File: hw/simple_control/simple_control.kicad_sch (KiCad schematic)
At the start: 1 part, among them J1 Screw_Terminal_01x02

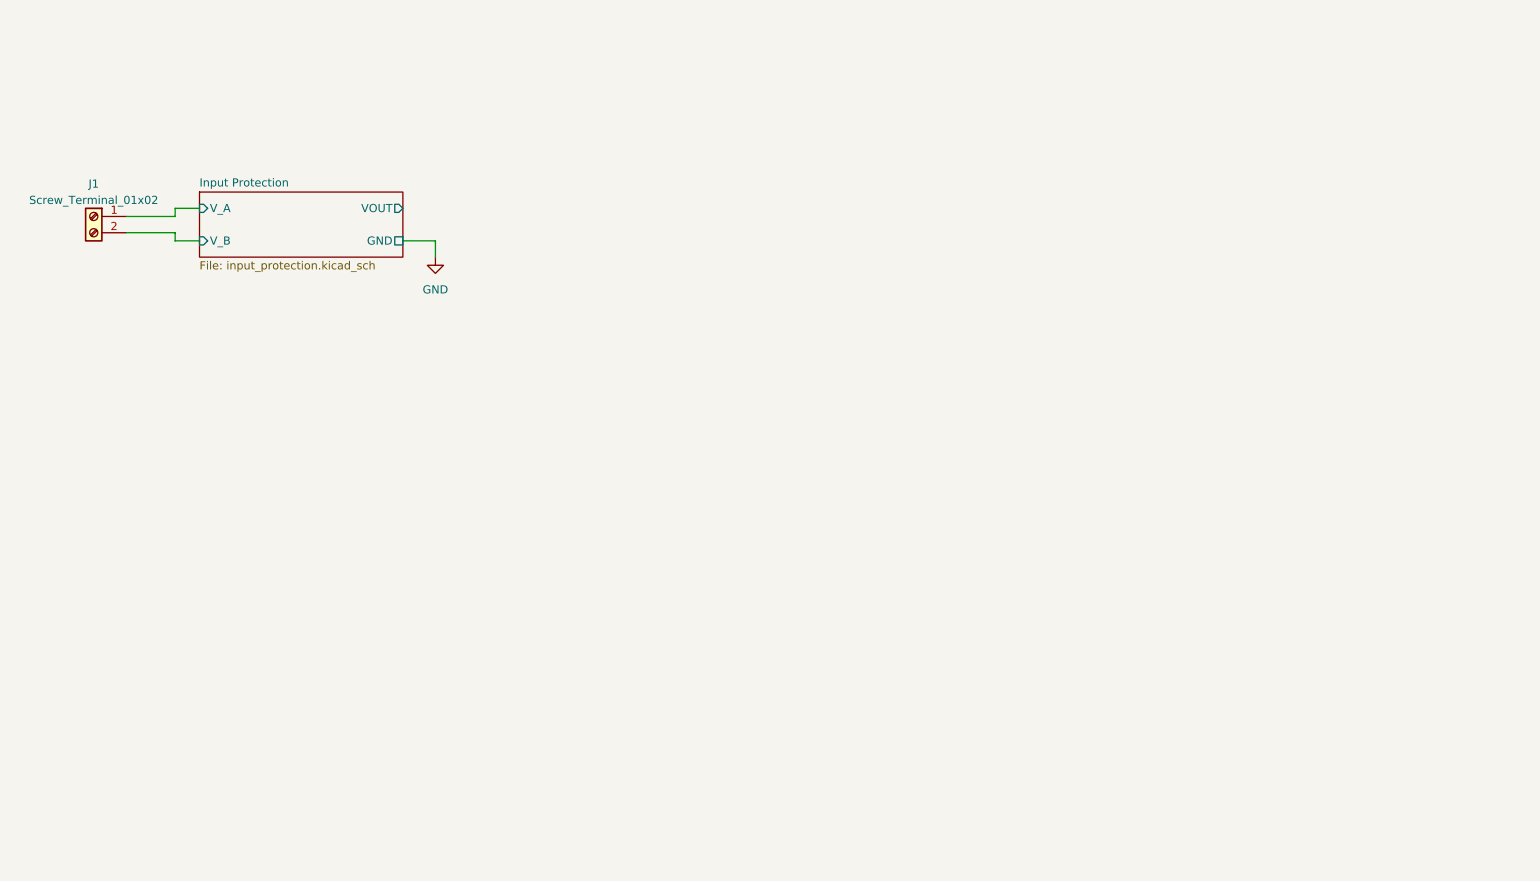
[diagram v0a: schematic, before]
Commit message: [hw] Add simple control LED driver
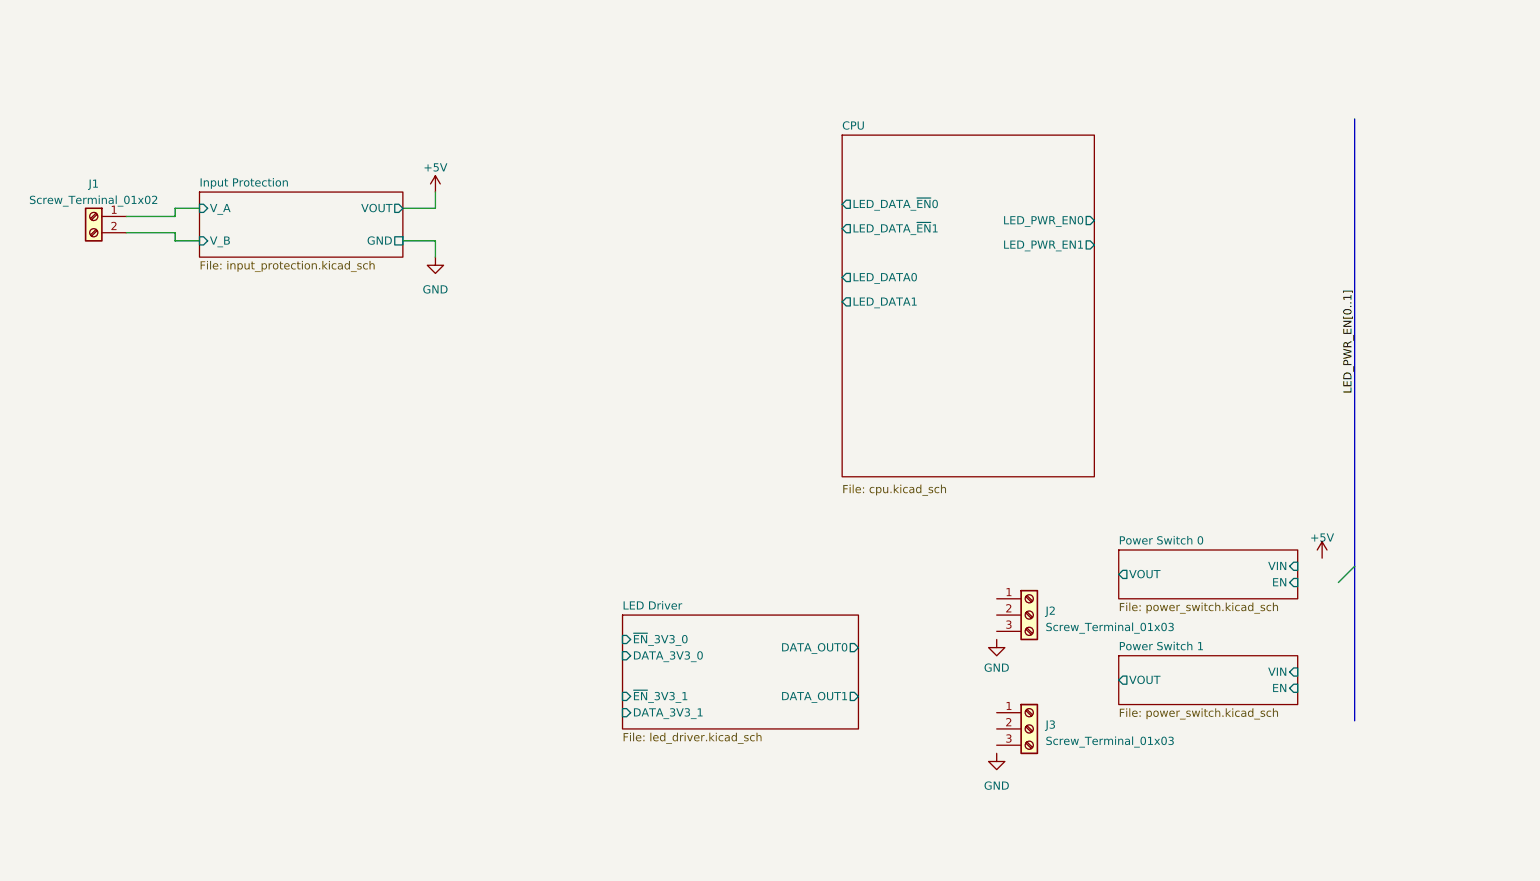
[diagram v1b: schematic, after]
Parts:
- added J2, J3: Screw_Terminal_01x03, symbol Connector:Screw_Terminal_01x03
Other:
- added sheet CPU (cpu.kicad_sch)
- added sheet LED Driver (led_driver.kicad_sch)
- added sheet Power Switch 0 (power_switch.kicad_sch)
- added sheet Power Switch 1 (power_switch.kicad_sch)

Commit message: [hw] Complete root schematics of simple control
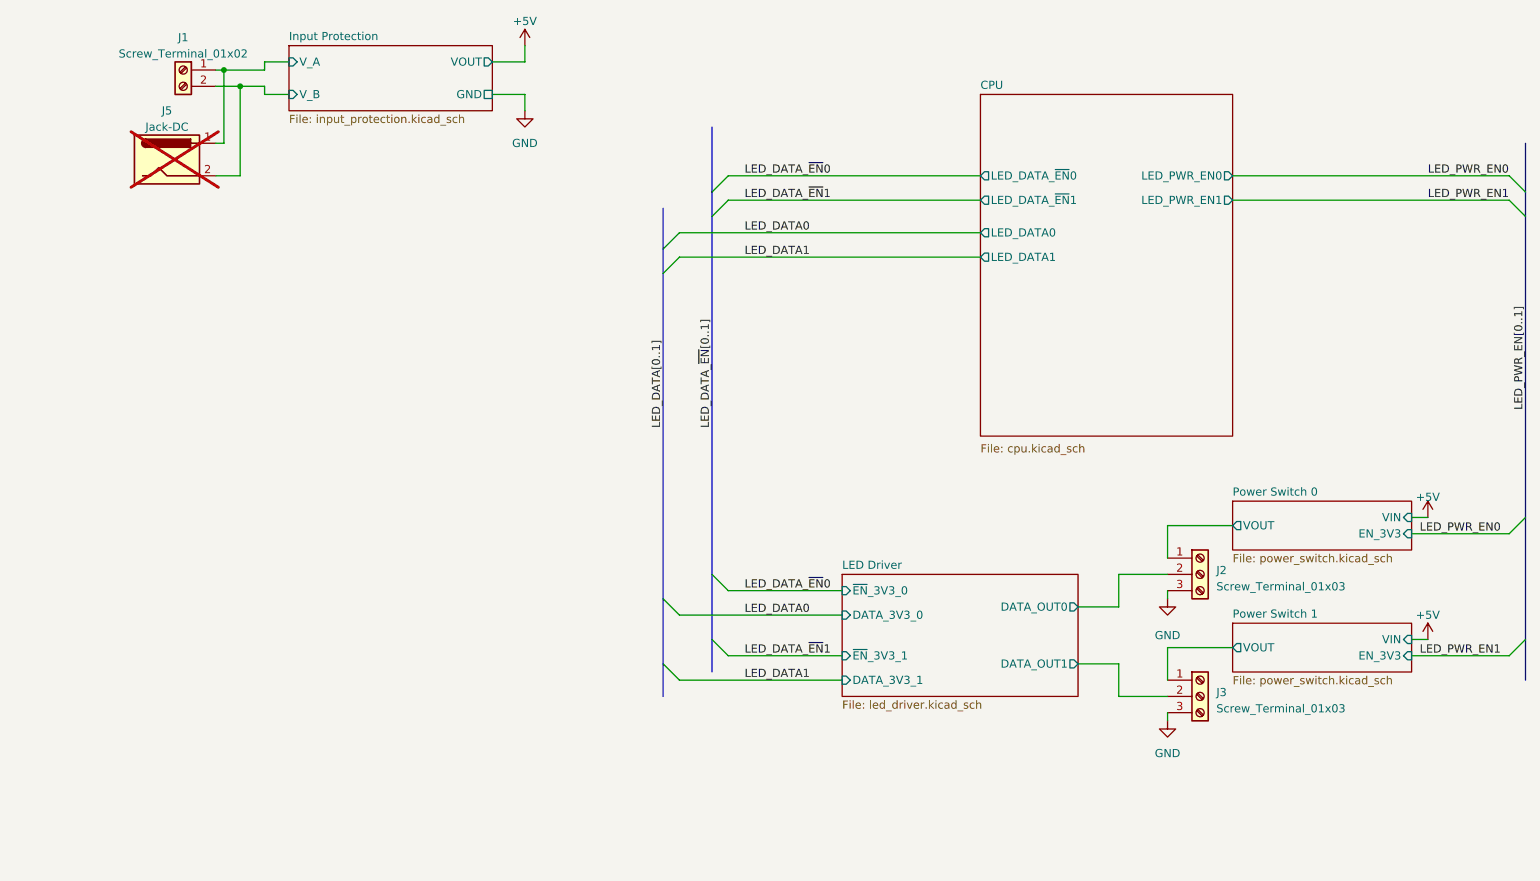
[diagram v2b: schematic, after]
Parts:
- added J5: Jack-DC, symbol Connector:Jack-DC
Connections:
- net GND: now also J2.3 (Pin_3), J3.3 (Pin_3)
- net Input Protection/V_A: now also J5.1
- net Input Protection/V_B: now also J5.2
- net LED Driver/DATA_OUT0: now also J2.2 (Pin_2)
- net LED Driver/DATA_OUT1: now also J3.2 (Pin_2)
- net Power Switch 0/VOUT: now also J2.1 (Pin_1)
- net Power Switch 1/VOUT: now also J3.1 (Pin_1)
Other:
- sheet Power Switch 0 ports: added EN_3V3; removed EN
- sheet Power Switch 1 ports: added EN_3V3; removed EN
- company: (none) -> Stefan Misik
- title: (none) -> WS2812 Simple Controller
- moved on the sheet: J1, J2, J3

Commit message: [hw] Wire some RPi Pico/Zero connections
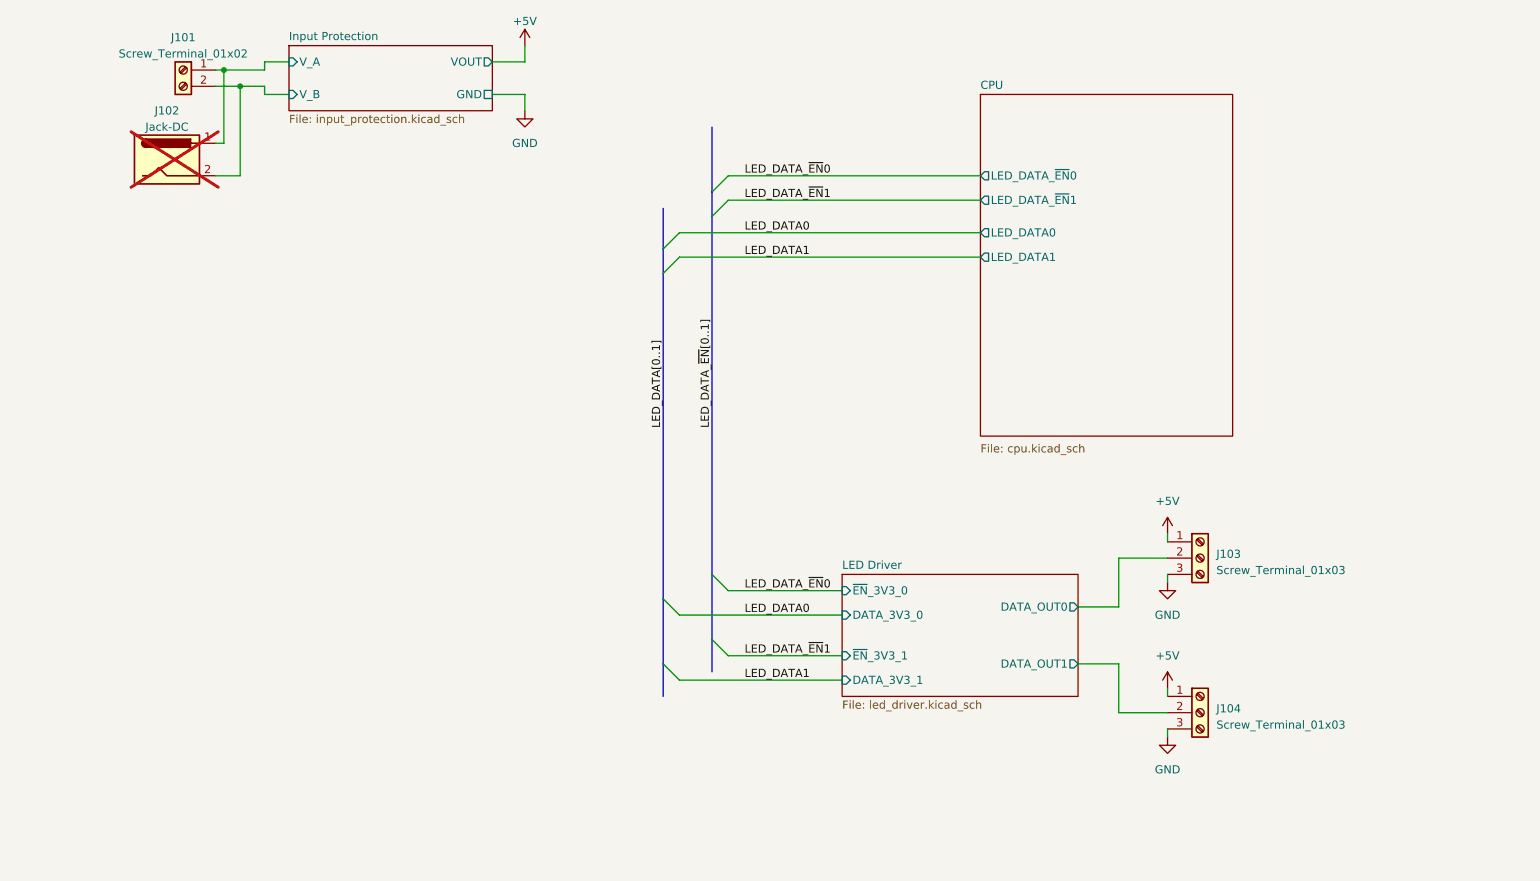
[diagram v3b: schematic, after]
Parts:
- renumbered J1 to J101, J5 to J102, J2 to J103, J3 to J104
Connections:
- net Power Switch 0/VOUT is gone; now on net +5V: J103.1 (Pin_1)
- net Power Switch 1/VOUT is gone; now on net +5V: J104.1 (Pin_1)
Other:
- removed sheet Power Switch 0
- removed sheet Power Switch 1
- sheet CPU ports: added none; removed LED_PWR_EN0, LED_PWR_EN1
- moved on the sheet: J103, J104

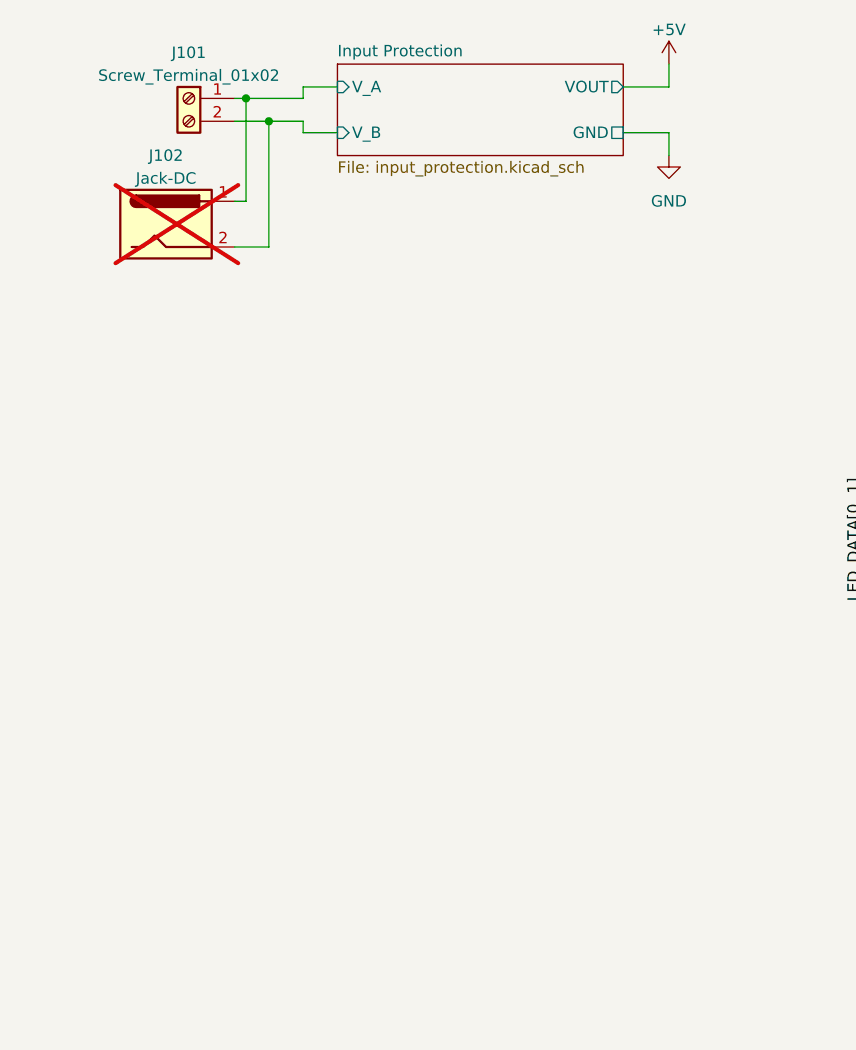
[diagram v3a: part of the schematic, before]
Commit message: [hw] Fix ERC issues, update RPi Pico library
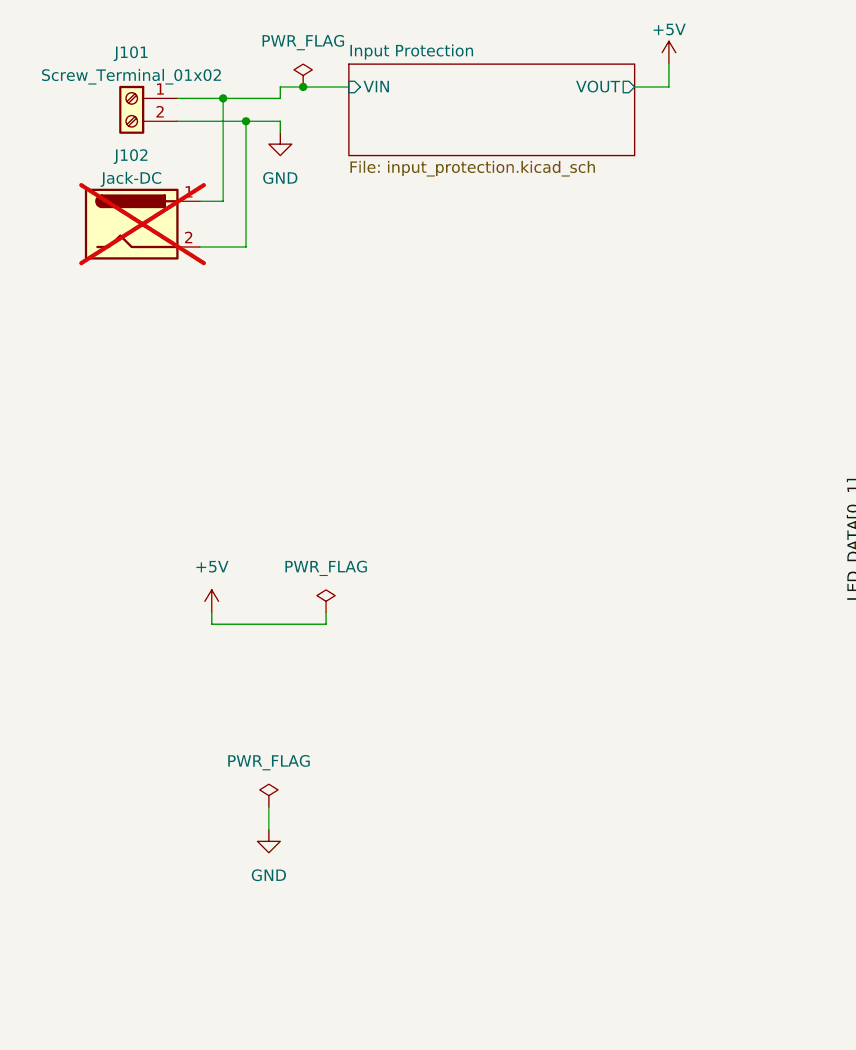
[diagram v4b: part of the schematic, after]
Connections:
- net Input Protection/V_B is gone; now on net GND: J101.2 (Pin_2), J102.2
- net Input Protection/V_A renamed Input Protection/VIN
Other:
- sheet Input Protection ports: added VIN; removed GND, V_A, V_B
- moved on the sheet: J101, J102

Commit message: chore(hw): assign footprints
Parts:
- J101: footprint (none) -> TerminalBlock_Phoenix:TerminalBlock_Phoenix_MKDS-1,5-2_1x02_P5.00mm_Horizontal
- J102: footprint (none) -> Connector_BarrelJack:BarrelJack_GCT_DCJ200-10-A_Horizontal; symbol Connector:Jack-DC -> Connector:Barrel_Jack_Switch; now in the parts list
- J103, J104: footprint (none) -> TerminalBlock_Phoenix:TerminalBlock_Phoenix_MKDS-1,5-3_1x03_P5.00mm_Horizontal
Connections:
- no-connect marks 0 -> 1
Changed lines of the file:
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@@
   (junction (at 50.8 45.72) (diameter 0) (color 0 0 0 0)
   )
+  (no_connect (at 39.37 60.96))
   (bus_entry (at 120.65 125.73) (size 2.54 2.54)
     (stroke (width 0) (type default))
@@
       (effects (font (size 1.27 1.27)) (justify left))
     )
-    (property "Footprint" "" (at 196.85 123.19 0)
+    (property "Footprint" "TerminalBlock_Phoenix:TerminalBlock_Phoenix_MKDS-1,5-3_1x03_P5.00mm_Horizontal" (at 196.85 123.19 0)
       (effects (font (size 1.27 1.27)) hide)
     )
@@
       (effects (font (size 1.27 1.27)))
     )
-    (property "Footprint" "" (at 31.75 46.99 0)
+    (property "Footprint" "TerminalBlock_Phoenix:TerminalBlock_Phoenix_MKDS-1,5-2_1x02_P5.00mm_Horizontal" (at 31.75 46.99 0)
       (effects (font (size 1.27 1.27)) hide)
     )
@@
   (symbol (lib_id "power:+5V") (at 40.64 104.14 0) (unit 1)
     (in_bom yes) (on_board yes) (dnp no) (fields_autoplaced)
-    (property "Reference" "#PWR0107" (at 40.64 107.95 0)
+    (property "Reference" "#PWR0103" (at 40.64 107.95 0)
       (effects (font (size 1.27 1.27)) hide)
     )
@@
       (project "simple_control"
         (path "/063164e8-0d2a-492b-8a61-e4fa4fbf06a6"
-          (reference "#PWR0107") (unit 1)
+          (reference "#PWR0103") (unit 1)
         )
       )
@@
   (symbol (lib_id "power:PWR_FLAG") (at 46.99 125.73 0) (unit 1)
     (in_bom yes) (on_board yes) (dnp no) (fields_autoplaced)
-    (property "Reference" "#FLG0105" (at 46.99 123.825 0)
+    (property "Reference" "#FLG0103" (at 46.99 123.825 0)
       (effects (font (size 1.27 1.27)) hide)
     )
@@
       (project "simple_control"
         (path "/063164e8-0d2a-492b-8a61-e4fa4fbf06a6"
-          (reference "#FLG0105") (unit 1)
+          (reference "#FLG0103") (unit 1)
         )
       )
@@
   (symbol (lib_id "power:+5V") (at 191.77 119.38 0) (unit 1)
     (in_bom yes) (on_board yes) (dnp no) (fields_autoplaced)
-    (property "Reference" "#PWR0103" (at 191.77 123.19 0)
+    (property "Reference" "#PWR0104" (at 191.77 123.19 0)
       (effects (font (size 1.27 1.27)) hide)
     )
@@
       (project "simple_control"
         (path "/063164e8-0d2a-492b-8a61-e4fa4fbf06a6"
-          (reference "#PWR0103") (unit 1)
+          (reference "#PWR0104") (unit 1)
         )
       )
@@
       (effects (font (size 1.27 1.27)) (justify left))
     )
-    (property "Footprint" "" (at 196.85 147.32 0)
+    (property "Footprint" "TerminalBlock_Phoenix:TerminalBlock_Phoenix_MKDS-1,5-3_1x03_P5.00mm_Horizontal" (at 196.85 147.32 0)
       (effects (font (size 1.27 1.27)) hide)
     )
@@
     )
   )
-  (symbol (lib_id "Connector:Jack-DC") (at 31.75 60.96 0) (unit 1)
-    (in_bom no) (on_board yes) (dnp yes) (fields_autoplaced)
+  (symbol (lib_id "Connector:Barrel_Jack_Switch") (at 31.75 60.96 0) (unit 1)
+    (in_bom yes) (on_board yes) (dnp yes) (fields_autoplaced)
     (property "Reference" "J102" (at 31.75 53.34 0)
       (effects (font (size 1.27 1.27)))
@@
       (effects (font (size 1.27 1.27)))
     )
-    (property "Footprint" "" (at 33.02 61.976 0)
+    (property "Footprint" "Connector_BarrelJack:BarrelJack_GCT_DCJ200-10-A_Horizontal" (at 33.02 61.976 0)
       (effects (font (size 1.27 1.27)) hide)
     )
@@
     (pin "1")
     (pin "2")
+    (pin "3")
     (instances
       (project "simple_control"
@@
   (symbol (lib_id "power:GND") (at 191.77 127 0) (unit 1)
     (in_bom yes) (on_board yes) (dnp no)
-    (property "Reference" "#PWR0104" (at 191.77 133.35 0)
+    (property "Reference" "#PWR0105" (at 191.77 133.35 0)
       (effects (font (size 1.27 1.27)) hide)
     )
@@
       (project "simple_control"
         (path "/063164e8-0d2a-492b-8a61-e4fa4fbf06a6"
-          (reference "#PWR0104") (unit 1)
+          (reference "#PWR0105") (unit 1)
         )
       )
@@
   (symbol (lib_id "power:GND") (at 191.77 151.13 0) (unit 1)
     (in_bom yes) (on_board yes) (dnp no)
-    (property "Reference" "#PWR0106" (at 191.77 157.48 0)
+    (property "Reference" "#PWR0108" (at 191.77 157.48 0)
       (effects (font (size 1.27 1.27)) hide)
     )
@@
       (project "simple_control"
         (path "/063164e8-0d2a-492b-8a61-e4fa4fbf06a6"
-          (reference "#PWR0106") (unit 1)
+          (reference "#PWR0108") (unit 1)
         )
       )
@@
   (symbol (lib_id "power:+5V") (at 191.77 143.51 0) (unit 1)
     (in_bom yes) (on_board yes) (dnp no)
-    (property "Reference" "#PWR0105" (at 191.77 147.32 0)
+    (property "Reference" "#PWR0107" (at 191.77 147.32 0)
       (effects (font (size 1.27 1.27)) hide)
     )
@@
       (project "simple_control"
         (path "/063164e8-0d2a-492b-8a61-e4fa4fbf06a6"
-          (reference "#PWR0105") (unit 1)
+          (reference "#PWR0107") (unit 1)
         )
       )
@@
   (symbol (lib_id "power:GND") (at 46.99 128.27 0) (unit 1)
     (in_bom yes) (on_board yes) (dnp no) (fields_autoplaced)
-    (property "Reference" "#PWR0109" (at 46.99 134.62 0)
+    (property "Reference" "#PWR0106" (at 46.99 134.62 0)
       (effects (font (size 1.27 1.27)) hide)
     )
@@
       (project "simple_control"
         (path "/063164e8-0d2a-492b-8a61-e4fa4fbf06a6"
-          (reference "#PWR0109") (unit 1)
+          (reference "#PWR0106") (unit 1)
         )
       )
@@
   (symbol (lib_id "power:PWR_FLAG") (at 53.34 104.14 0) (unit 1)
     (in_bom yes) (on_board yes) (dnp no) (fields_autoplaced)
-    (property "Reference" "#FLG0103" (at 53.34 102.235 0)
+    (property "Reference" "#FLG0102" (at 53.34 102.235 0)
       (effects (font (size 1.27 1.27)) hide)
     )
@@
       (project "simple_control"
         (path "/063164e8-0d2a-492b-8a61-e4fa4fbf06a6"
-          (reference "#FLG0103") (unit 1)
-        )
-      )
+          (reference "#FLG0102") (unit 1)
+        )
+      )
